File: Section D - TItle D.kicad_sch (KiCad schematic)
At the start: 5 parts, among them Q2 CSD18534Q5A

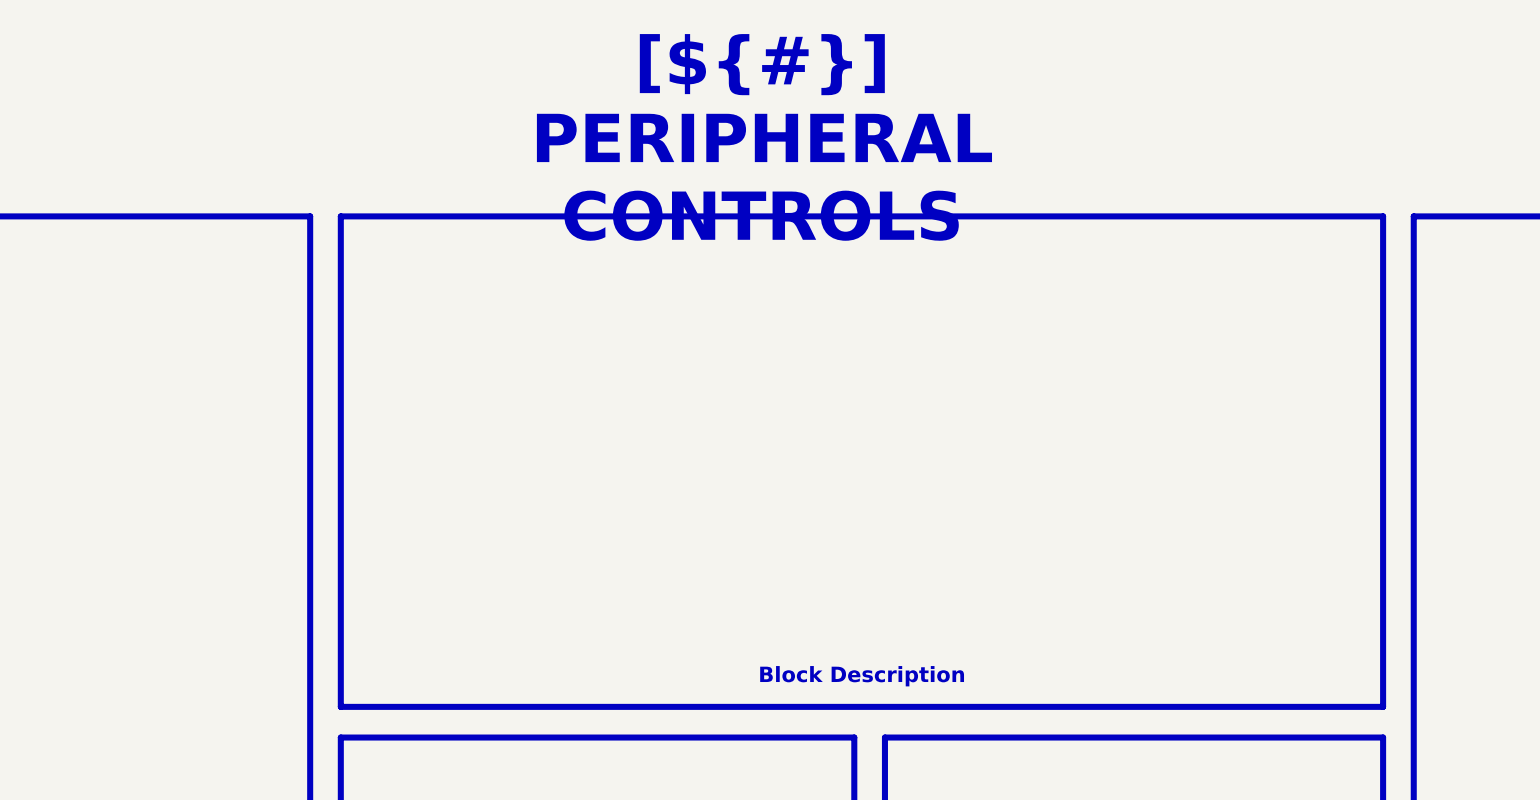
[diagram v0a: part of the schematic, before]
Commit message: [SCHEMATICS] Ajout de convertisseur + autres
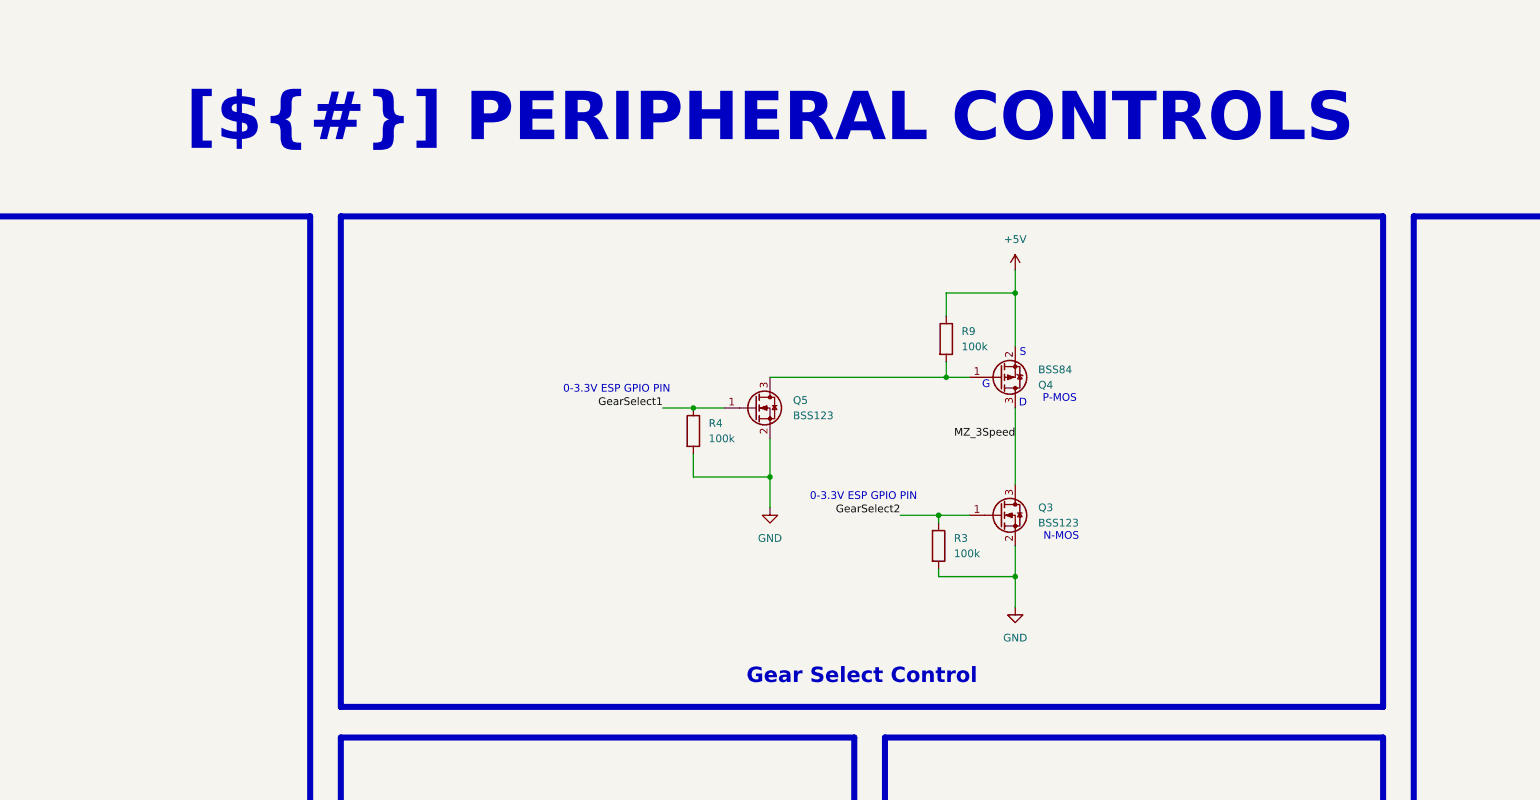
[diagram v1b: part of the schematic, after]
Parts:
- added Q3, Q5: BSS123, Package_TO_SOT_SMD:SOT-23, symbol Transistor_FET:BSS123
- added Q4: BSS84, Package_TO_SOT_SMD:SOT-23, symbol Transistor_FET:BSS84
- added R3, R4, R9: 100k, Resistor_SMD:R_0603_1608Metric_Pad0.98x0.95mm_HandSolder, symbol Device:R
- D2: Manufacturer Part Number (none) -> BZT52C3V3
- Q2: Manufacturer Part Number (none) -> CBG322513U601T
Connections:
- net GND: now also Q3.2 (S), Q5.2 (S), R3.2, R4.2
- new net: Q4.1 (G), Q5.3 (D), R9.2
- new net +5V: Q4.2 (S), R9.1
- new net GearSelect1: Q5.1 (G), R4.1
- new net GearSelect2: Q3.1 (G), R3.1
- new net MZ_3Speed: Q3.3 (D), Q4.3 (D)
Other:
- note added: "0-3.3V ESP GPIO PIN"
- note added: "D"
- note added: "G"
- note added: "N-MOS"
- note added: "P-MOS"
- note added: "S"
